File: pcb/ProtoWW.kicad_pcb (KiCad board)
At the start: 2 copper layers, 160 x 120 mm, 1178 parts

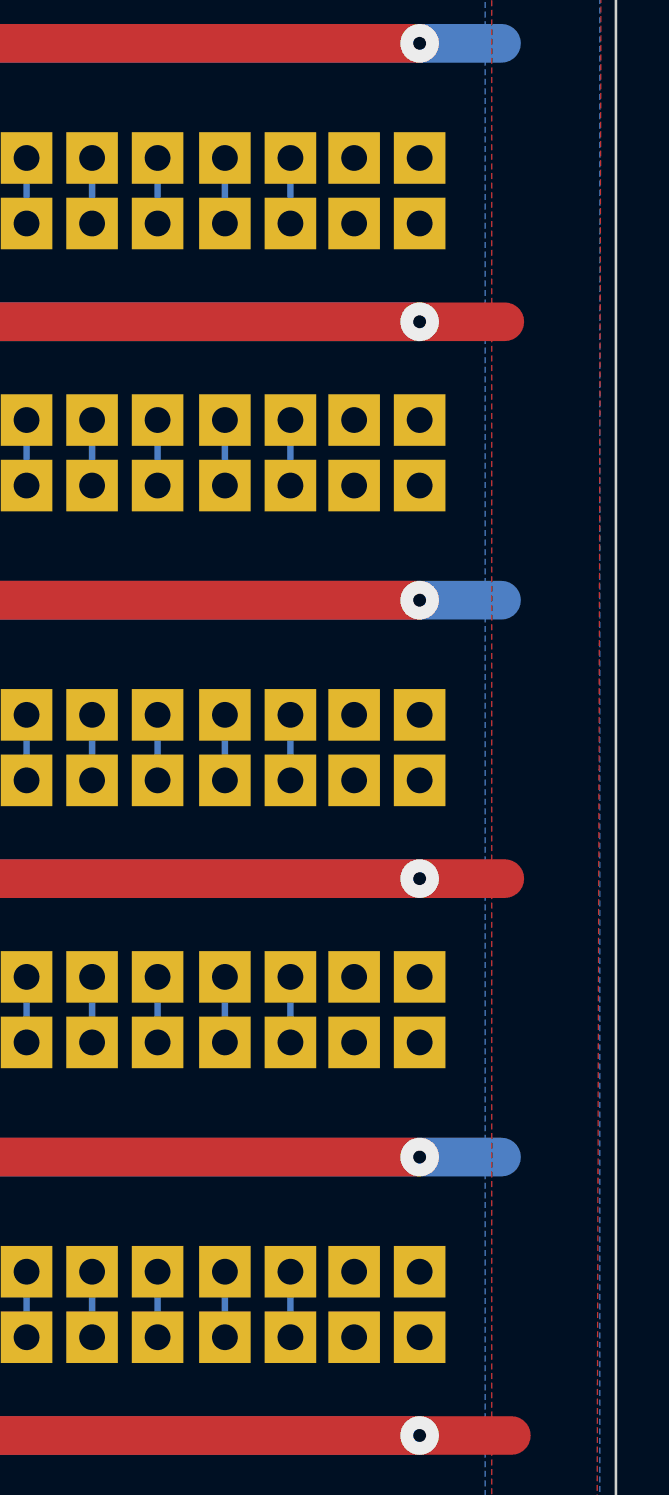
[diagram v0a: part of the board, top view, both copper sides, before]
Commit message: Added a few missing tracks
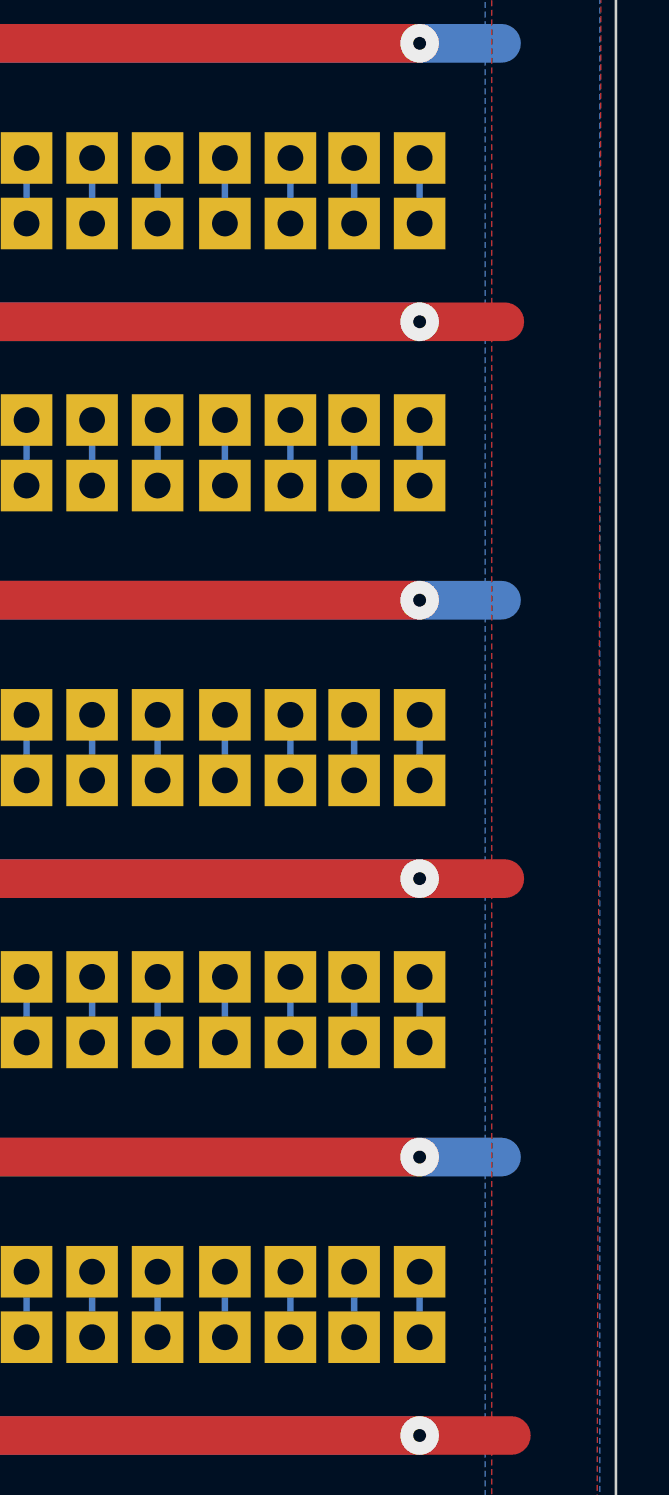
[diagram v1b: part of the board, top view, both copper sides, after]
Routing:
- net (no net): track 1955.7 -> 1981.1 mm
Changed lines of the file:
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@@
   (segment (start 179.37 112.86) (end 179.37 115.4) (width 0.25) (layer "B.Cu") (net 0))
   (segment (start 171.75 79.84) (end 171.75 82.38) (width 0.25) (layer "B.Cu") (net 0))
+  (segment (start 225.09 91.27) (end 225.09 93.81) (width 0.25) (layer "B.Cu") (net 0))
   (segment (start 136.19 123.02) (end 136.19 125.56) (width 0.25) (layer "B.Cu") (net 0))
   (segment (start 159.05 134.45) (end 159.05 136.99) (width 0.25) (layer "B.Cu") (net 0))
@@
   (segment (start 103.17 144.61) (end 103.17 147.15) (width 0.25) (layer "B.Cu") (net 0))
   (segment (start 214.93 69.68) (end 214.93 72.22) (width 0.25) (layer "B.Cu") (net 0))
+  (segment (start 225.09 134.45) (end 225.09 136.99) (width 0.25) (layer "B.Cu") (net 0))
   (segment (start 217.54 69.68) (end 217.54 72.22) (width 0.25) (layer "B.Cu") (net 0))
   (segment (start 179.37 101.43) (end 179.37 103.97) (width 0.25) (layer "B.Cu") (net 0))
@@
   (segment (start 153.97 134.45) (end 153.97 136.99) (width 0.25) (layer "B.Cu") (net 0))
   (segment (start 143.81 134.45) (end 143.81 136.99) (width 0.25) (layer "B.Cu") (net 0))
+  (segment (start 225.09 123.02) (end 225.09 125.56) (width 0.25) (layer "B.Cu") (net 0))
   (segment (start 146.35 123.02) (end 146.35 125.56) (width 0.25) (layer "B.Cu") (net 0))
   (segment (start 131.11 101.43) (end 131.11 103.97) (width 0.25) (layer "B.Cu") (net 0))
@@
   (segment (start 123.49 144.61) (end 123.49 147.15) (width 0.25) (layer "B.Cu") (net 0))
   (segment (start 176.76 152.23) (end 176.76 154.77) (width 0.25) (layer "B.Cu") (net 0))
+  (segment (start 222.55 123.02) (end 222.55 125.56) (width 0.25) (layer "B.Cu") (net 0))
   (segment (start 136.19 101.43) (end 136.19 103.97) (width 0.25) (layer "B.Cu") (net 0))
   (segment (start 184.45 91.27) (end 184.45 93.81) (width 0.25) (layer "B.Cu") (net 0))
@@
   (segment (start 214.93 134.45) (end 214.93 136.99) (width 0.25) (layer "B.Cu") (net 0))
   (segment (start 209.85 101.43) (end 209.85 103.97) (width 0.25) (layer "B.Cu") (net 0))
+  (segment (start 222.55 91.27) (end 222.55 93.81) (width 0.25) (layer "B.Cu") (net 0))
   (segment (start 105.71 79.84) (end 105.71 82.38) (width 0.25) (layer "B.Cu") (net 0))
   (segment (start 138.73 69.68) (end 138.73 72.22) (width 0.25) (layer "B.Cu") (net 0))
@@
   (segment (start 166.67 79.84) (end 166.67 82.38) (width 0.25) (layer "B.Cu") (net 0))
   (segment (start 108.25 134.45) (end 108.25 136.99) (width 0.25) (layer "B.Cu") (net 0))
+  (segment (start 225.09 101.43) (end 225.09 103.97) (width 0.25) (layer "B.Cu") (net 0))
   (segment (start 202.23 69.68) (end 202.23 72.22) (width 0.25) (layer "B.Cu") (net 0))
   (segment (start 197.15 69.68) (end 197.15 72.22) (width 0.25) (layer "B.Cu") (net 0))
@@
   (segment (start 220.08 69.68) (end 220.08 72.22) (width 0.25) (layer "B.Cu") (net 0))
   (segment (start 156.51 134.45) (end 156.51 136.99) (width 0.25) (layer "B.Cu") (net 0))
+  (segment (start 222.55 112.86) (end 222.55 115.4) (width 0.25) (layer "B.Cu") (net 0))
   (segment (start 148.89 79.84) (end 148.89 82.38) (width 0.25) (layer "B.Cu") (net 0))
   (segment (start 146.35 48.09) (end 146.35 50.63) (width 0.25) (layer "B.Cu") (net 0))
@@
   (segment (start 113.33 91.27) (end 113.33 93.81) (width 0.25) (layer "B.Cu") (net 0))
   (segment (start 110.79 112.86) (end 110.79 115.4) (width 0.25) (layer "B.Cu") (net 0))
+  (segment (start 222.55 134.45) (end 222.55 136.99) (width 0.25) (layer "B.Cu") (net 0))
   (segment (start 138.73 123.02) (end 138.73 125.56) (width 0.25) (layer "B.Cu") (net 0))
   (segment (start 138.66 152.23) (end 138.66 154.77) (width 0.25) (layer "B.Cu") (net 0))
@@
   (segment (start 220.08 144.61) (end 220.08 147.15) (width 0.25) (layer "B.Cu") (net 0))
   (segment (start 143.81 91.27) (end 143.81 93.81) (width 0.25) (layer "B.Cu") (net 0))
+  (segment (start 225.09 112.86) (end 225.09 115.4) (width 0.25) (layer "B.Cu") (net 0))
   (segment (start 148.89 91.27) (end 148.89 93.81) (width 0.25) (layer "B.Cu") (net 0))
   (segment (start 118.41 91.27) (end 118.41 93.81) (width 0.25) (layer "B.Cu") (net 0))
@@
   (segment (start 164.13 69.68) (end 164.13 72.22) (width 0.25) (layer "B.Cu") (net 0))
   (segment (start 189.46 152.23) (end 189.46 154.77) (width 0.25) (layer "B.Cu") (net 0))
+  (segment (start 222.55 101.43) (end 222.55 103.97) (width 0.25) (layer "B.Cu") (net 0))
   (segment (start 105.71 134.45) (end 105.71 136.99) (width 0.25) (layer "B.Cu") (net 0))
   (segment (start 217.54 123.02) (end 217.54 125.56) (width 0.25) (layer "B.Cu") (net 0))
